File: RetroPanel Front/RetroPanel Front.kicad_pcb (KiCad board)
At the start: 2 copper layers, 100 x 22.5 mm, 17 parts, among them J1 Front Panel, M1 Mounting_Pin, M10 Mounting_Pad, M2 Mounting_Pin, M3 Mounting_Pin, M4 Mounting_Pin, M5 Mounting_Pad, M7 Mounting_Pad, M9 Mounting_Pad, SW1 TURBO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

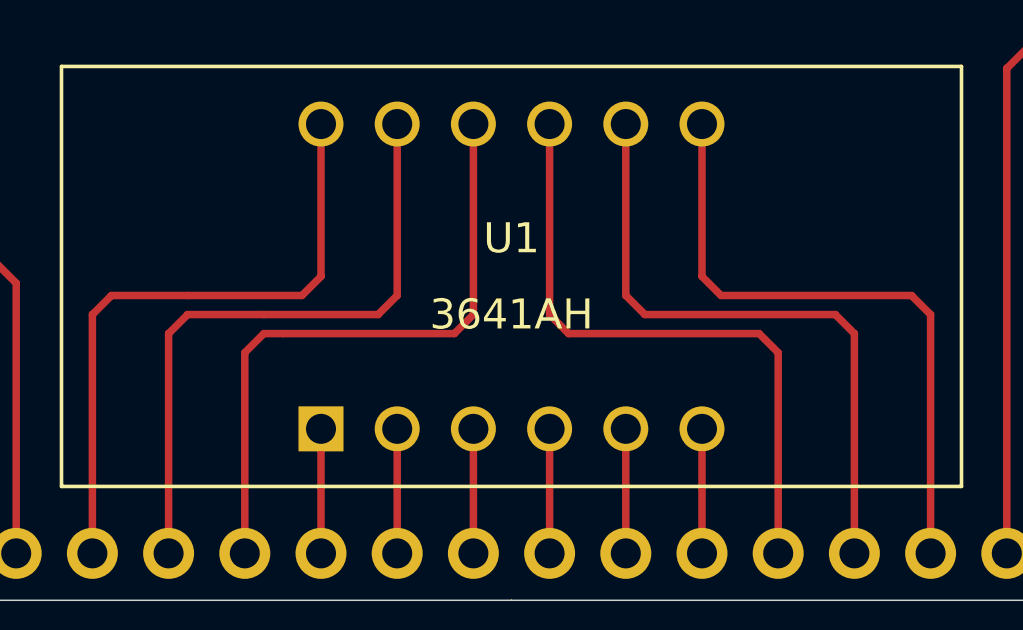
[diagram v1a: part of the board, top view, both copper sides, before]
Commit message: Can use both types of displays
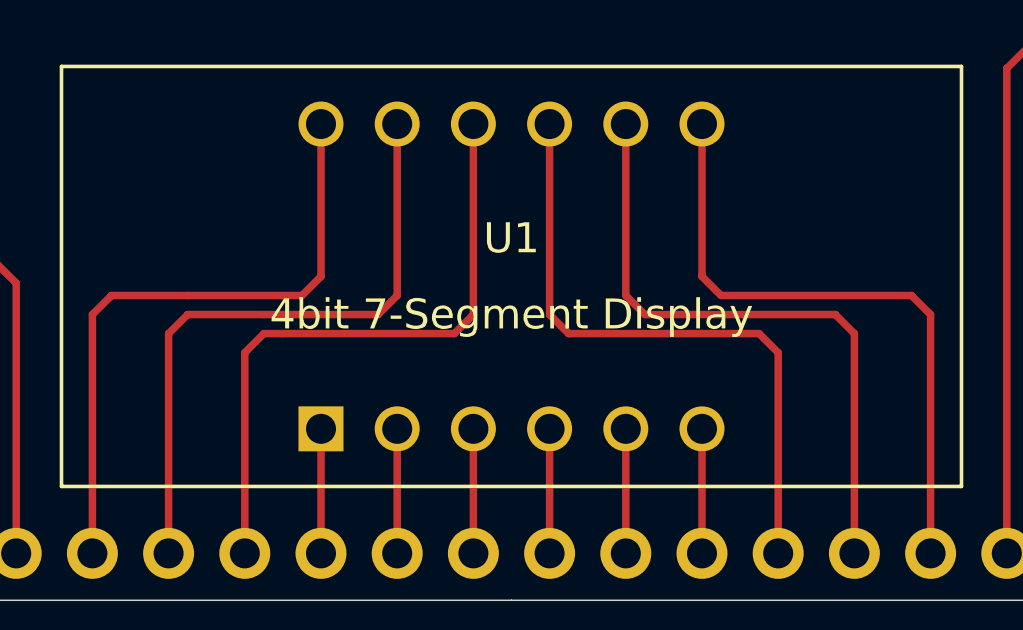
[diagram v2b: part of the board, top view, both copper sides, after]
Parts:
- U1: value 3641AH -> 4bit 7-Segment Display

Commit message: Fixed RS-232 connector and export files for second prototype
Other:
- board text added: "JLCJLCJLCJLC"
